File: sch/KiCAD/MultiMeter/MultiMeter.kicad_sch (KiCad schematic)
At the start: 27 parts, among them J1 Conn_01x02_Male, J2 Conn_01x02_Male, J3 Conn_01x03_Male, J4 Conn_01x03_Male, J5 Conn_01x02_Female, J6 Conn_01x15, J7 Conn_01x15, J8 Conn_01x08_Female, Q1 2SC1815, Q2 2SC1815

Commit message: 回路図修正
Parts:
- added J9: (no value), symbol Connector:Conn_01x02_Male
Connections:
- net GNDPWR: now also J9.2 (Pin_2)
- net +12V: now reaches A1.30 (VIN), J7.15 (Pin_15)
- net +12V: now also J9.1 (Pin_1)
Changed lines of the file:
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@@
   (junction (at 83.82 52.07) (diameter 0) (color 0 0 0 0)
   )
+  (junction (at 111.76 26.67) (diameter 0) (color 0 0 0 0)
+  )
   (junction (at 133.35 72.39) (diameter 0) (color 0 0 0 0)
   )
@@
     (stroke (width 0) (type default) (color 0 0 0 0))
   )
+  (wire (pts (xy 110.49 176.53) (xy 110.49 167.64))
+    (stroke (width 0) (type default) (color 0 0 0 0))
+  )
   (wire (pts (xy 116.84 25.4) (xy 139.7 25.4))
     (stroke (width 0) (type default) (color 0 0 0 0))
@@
     (stroke (width 0) (type default) (color 0 0 0 0))
   )
+  (wire (pts (xy 110.49 167.64) (xy 121.92 167.64))
+    (stroke (width 0) (type default) (color 0 0 0 0))
+  )
   (wire (pts (xy 50.8 34.29) (xy 50.8 45.72))
     (stroke (width 0) (type default) (color 0 0 0 0))
@@
     (stroke (width 0) (type default) (color 0 0 0 0))
   )
+  (wire (pts (xy 85.09 20.32) (xy 85.09 22.86))
+    (stroke (width 0) (type default) (color 0 0 0 0))
+  )
   (wire (pts (xy 133.35 72.39) (xy 149.86 72.39))
     (stroke (width 0) (type default) (color 0 0 0 0))
@@
     (stroke (width 0) (type default) (color 0 0 0 0))
   )
+  (wire (pts (xy 111.76 20.32) (xy 85.09 20.32))
+    (stroke (width 0) (type default) (color 0 0 0 0))
+  )
   (wire (pts (xy 173.99 67.31) (xy 173.99 78.74))
     (stroke (width 0) (type default) (color 0 0 0 0))
@@
     (stroke (width 0) (type default) (color 0 0 0 0))
   )
+  (wire (pts (xy 97.79 176.53) (xy 97.79 165.1))
+    (stroke (width 0) (type default) (color 0 0 0 0))
+  )
   (wire (pts (xy 97.79 80.01) (xy 97.79 106.68))
     (stroke (width 0) (type default) (color 0 0 0 0))
@@
     (stroke (width 0) (type default) (color 0 0 0 0))
   )
+  (wire (pts (xy 111.76 26.67) (xy 111.76 20.32))
+    (stroke (width 0) (type default) (color 0 0 0 0))
+  )
   (wire (pts (xy 44.45 62.23) (xy 44.45 60.96))
+    (stroke (width 0) (type default) (color 0 0 0 0))
+  )
+  (wire (pts (xy 97.79 165.1) (xy 121.92 165.1))
     (stroke (width 0) (type default) (color 0 0 0 0))
   )
@@
     (pin "2")
   )
+  (symbol (lib_id "power:+12V") (at 97.79 176.53 0) (mirror x) (unit 1)
+    (in_bom yes) (on_board yes) (fields_autoplaced)
+    (property "Reference" "#PWR0117" (id 0) (at 97.79 172.72 0)
+      (effects (font (size 1.27 1.27)) hide)
+    )
+    (property "Value" "+12V" (id 1) (at 97.79 181.61 0))
+    (property "Footprint" "" (id 2) (at 97.79 176.53 0)
+      (effects (font (size 1.27 1.27)) hide)
+    )
+    (property "Datasheet" "" (id 3) (at 97.79 176.53 0)
+      (effects (font (size 1.27 1.27)) hide)
+    )
+    (pin "1")
+  )
   (symbol (lib_id "power:GNDPWR") (at 58.42 77.47 0) (unit 1)
     (in_bom yes) (on_board yes) (fields_autoplaced)
@@
     )
     (property "Datasheet" "" (id 3) (at 173.99 88.9 0)
+      (effects (font (size 1.27 1.27)) hide)
+    )
+    (pin "1")
+  )
+  (symbol (lib_id "power:+12V") (at 85.09 22.86 0) (mirror x) (unit 1)
+    (in_bom yes) (on_board yes) (fields_autoplaced)
+    (property "Reference" "#PWR0116" (id 0) (at 85.09 19.05 0)
+      (effects (font (size 1.27 1.27)) hide)
+    )
+    (property "Value" "+12V" (id 1) (at 85.09 27.94 0))
+    (property "Footprint" "" (id 2) (at 85.09 22.86 0)
+      (effects (font (size 1.27 1.27)) hide)
+    )
+    (property "Datasheet" "" (id 3) (at 85.09 22.86 0)
       (effects (font (size 1.27 1.27)) hide)
     )
@@
     (pin "1")
   )
+  (symbol (lib_id "power:GNDPWR") (at 110.49 176.53 0) (unit 1)
+    (in_bom yes) (on_board yes) (fields_autoplaced)
+    (property "Reference" "#PWR0118" (id 0) (at 110.49 181.61 0)
+      (effects (font (size 1.27 1.27)) hide)
+    )
+    (property "Value" "GNDPWR" (id 1) (at 110.363 181.61 0))
+    (property "Footprint" "" (id 2) (at 110.49 177.8 0)
+      (effects (font (size 1.27 1.27)) hide)
+    )
+    (property "Datasheet" "" (id 3) (at 110.49 177.8 0)
+      (effects (font (size 1.27 1.27)) hide)
+    )
+    (pin "1")
+  )
   (symbol (lib_id "power:+5V") (at 154.94 90.17 180) (unit 1)
     (in_bom yes) (on_board yes) (fields_autoplaced)
@@
     (pin "2")
   )
+  (symbol (lib_id "Connector:Conn_01x02_Male") (at 127 165.1 0) (mirror y) (unit 1)
+    (in_bom yes) (on_board yes) (fields_autoplaced)
+    (property "Reference" "J9" (id 0) (at 128.27 165.0999 0)
+      (effects (font (size 1.27 1.27)) (justify right))
+    )
+    (property "Value" "" (id 1) (at 128.27 167.6399 0)
+      (effects (font (size 1.27 1.27)) (justify right))
+    )
+    (property "Footprint" "" (id 2) (at 127 165.1 0)
+      (effects (font (size 1.27 1.27)) hide)
+    )
+    (property "Datasheet" "~" (id 3) (at 127 165.1 0)
+      (effects (font (size 1.27 1.27)) hide)
+    )
+    (pin "1")
+    (pin "2")
+  )
   (symbol (lib_id "power:+5V") (at 171.45 137.16 180) (unit 1)
     (in_bom yes) (on_board yes) (fields_autoplaced)
@@
       (reference "#PWR0115") (unit 1) (value "GNDPWR") (footprint "")
     )
+    (path "/572bf966-40b4-4074-84f8-0470619143e0"
+      (reference "#PWR0116") (unit 1) (value "+12V") (footprint "")
+    )
+    (path "/2764df4e-6524-4e92-b3c2-377361d2725a"
+      (reference "#PWR0117") (unit 1) (value "+12V") (footprint "")
+    )
+    (path "/bcc17d3a-2a6b-4226-83a3-ee2299dfa9ff"
+      (reference "#PWR0118") (unit 1) (value "GNDPWR") (footprint "")
+    )
     (path "/b8413942-d6c5-419c-abde-ad0808ce4040"
       (reference "A1") (unit 1) (value "Arduino_Nano_v3.x") (footprint "Module:Arduino_Nano")
@@
       (reference "J8") (unit 1) (value "Conn_01x08_Female") (footprint "Connector_JST:JST_XH_B8B-XH-A_1x08_P2.50mm_Vertical")
     )
+    (path "/cd4406c8-1d31-4759-9e62-d689d76eb5ee"
+      (reference "J9") (unit 1) (value "Conn_01x02_Female") (footprint "Connector_Molex:Molex_KK-254_AE-6410-02A_1x02_P2.54mm_Vertical")
+    )
     (path "/6516d9f9-5a5c-40a3-bbc8-e5224e1e784c"

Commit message: 回路図修正
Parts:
- removed R10: 7K ohm, Resistor_THT:R_Axial_DIN0204_L3.6mm_D1.6mm_P7.62mm_Horizontal, symbol Device:R
- removed R11: 5K ohm, Resistor_THT:R_Axial_DIN0204_L3.6mm_D1.6mm_P7.62mm_Horizontal, symbol Device:R
- removed TP1, TP2: TestPoint, MountingHole:MountingHole_2.2mm_M2_DIN965_Pad, symbol Connector:TestPoint
- J5: value Conn_01x02_Female -> (none); footprint Connector_Molex:Molex_KK-254_AE-6410-02A_1x02_P2.54mm_Vertical -> (none); symbol Connector:Conn_01x02_Female -> Connector:Conn_01x03_Female
- J9: value (none) -> Conn_01x02_Female; footprint (none) -> Connector_Molex:Molex_KK-254_AE-6410-02A_1x02_P2.54mm_Vertical; symbol Connector:Conn_01x02_Male -> Connector:Conn_01x03_Female
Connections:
- net +12V: now also J9.2 (Pin_2), RV1.1; no longer J9.1 (Pin_1)
- net +5V: no longer RV1.1
- net GNDPWR: now also J9.3 (Pin_3), Q2.3 (B), R9.2; no longer J9.2 (Pin_2)
- net at A1.23 (A4), J7.8 (Pin_8), J8.4 (Pin_4): no longer J4.2 (Pin_2)
- net at A1.25 (A6), J7.10 (Pin_10): now also J4.2 (Pin_2)
- net at A1.26 (A7), J7.11 (Pin_11): now also J5.3 (Pin_3)
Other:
- moved on the sheet: A1, D5, J1, J2, J3, J4, J6, J7, J8, JP1, Q1, Q2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

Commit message: 回路図修正
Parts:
- J5: value (none) -> Conn_01x03_Female; footprint (none) -> Connector_Molex:Molex_KK-254_AE-6410-03A_1x03_P2.54mm_Vertical
- J9: value Conn_01x02_Female -> (none); footprint Connector_Molex:Molex_KK-254_AE-6410-02A_1x02_P2.54mm_Vertical -> (none); symbol Connector:Conn_01x03_Female -> Connector:Conn_01x02_Female
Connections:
- net +12V: now also J9.1 (Pin_1); no longer J9.2 (Pin_2)
- net GNDPWR: now also J9.2 (Pin_2); no longer J9.3 (Pin_3)
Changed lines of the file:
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@@
     (in_bom yes) (on_board yes)
     (property "Reference" "J5" (id 0) (at 33.655 59.69 0))
-    (property "Value" "" (id 1) (at 33.02 55.88 0))
-    (property "Footprint" "" (id 2) (at 33.02 64.77 0)
+    (property "Value" "Conn_01x03_Female" (id 1) (at 33.02 55.88 0))
+    (property "Footprint" "Connector_Molex:Molex_KK-254_AE-6410-03A_1x03_P2.54mm_Vertical" (id 2) (at 33.02 64.77 0)
       (effects (font (size 1.27 1.27)) hide)
     )
@@
     (pin "2")
   )
-  (symbol (lib_id "Connector:Conn_01x03_Female") (at 127 165.1 0) (unit 1)
+  (symbol (lib_id "Connector:Conn_01x02_Female") (at 127 165.1 0) (unit 1)
     (in_bom yes) (on_board yes)
     (property "Reference" "J9" (id 0) (at 128.27 158.75 0)
       (effects (font (size 1.27 1.27)) (justify right))
     )
-    (property "Value" "Conn_01x02_Female" (id 1) (at 137.16 172.72 0)
+    (property "Value" "" (id 1) (at 137.16 172.72 0)
       (effects (font (size 1.27 1.27)) (justify right))
     )
-    (property "Footprint" "Connector_Molex:Molex_KK-254_AE-6410-02A_1x02_P2.54mm_Vertical" (id 2) (at 127 165.1 0)
+    (property "Footprint" "" (id 2) (at 127 165.1 0)
       (effects (font (size 1.27 1.27)) hide)
     )
@@
     (pin "1")
     (pin "2")
-    (pin "3")
   )
   (symbol (lib_id "power:+5V") (at 187.96 142.24 180) (unit 1)

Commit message: 回路図更新
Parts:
- added J10: (no value), symbol Connector:Conn_01x04_Female
- J8: value Conn_01x08_Female -> (none); footprint Connector_JST:JST_XH_B8B-XH-A_1x08_P2.50mm_Vertical -> (none)
- J9: value (none) -> Conn_01x02_Female; footprint (none) -> Connector_Molex:Molex_KK-254_AE-6410-02A_1x02_P2.54mm_Vertical
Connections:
- net +5V: now also J10.1 (Pin_1)
- net GNDPWR: now also J10.4 (Pin_4)
- net at A1.1 (D1/TX), J6.1 (Pin_1): now also J10.3 (Pin_3)
- net at A1.2 (D0/RX), J6.2 (Pin_2): now also J10.2 (Pin_2)
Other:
- moved on the sheet: D5, R5

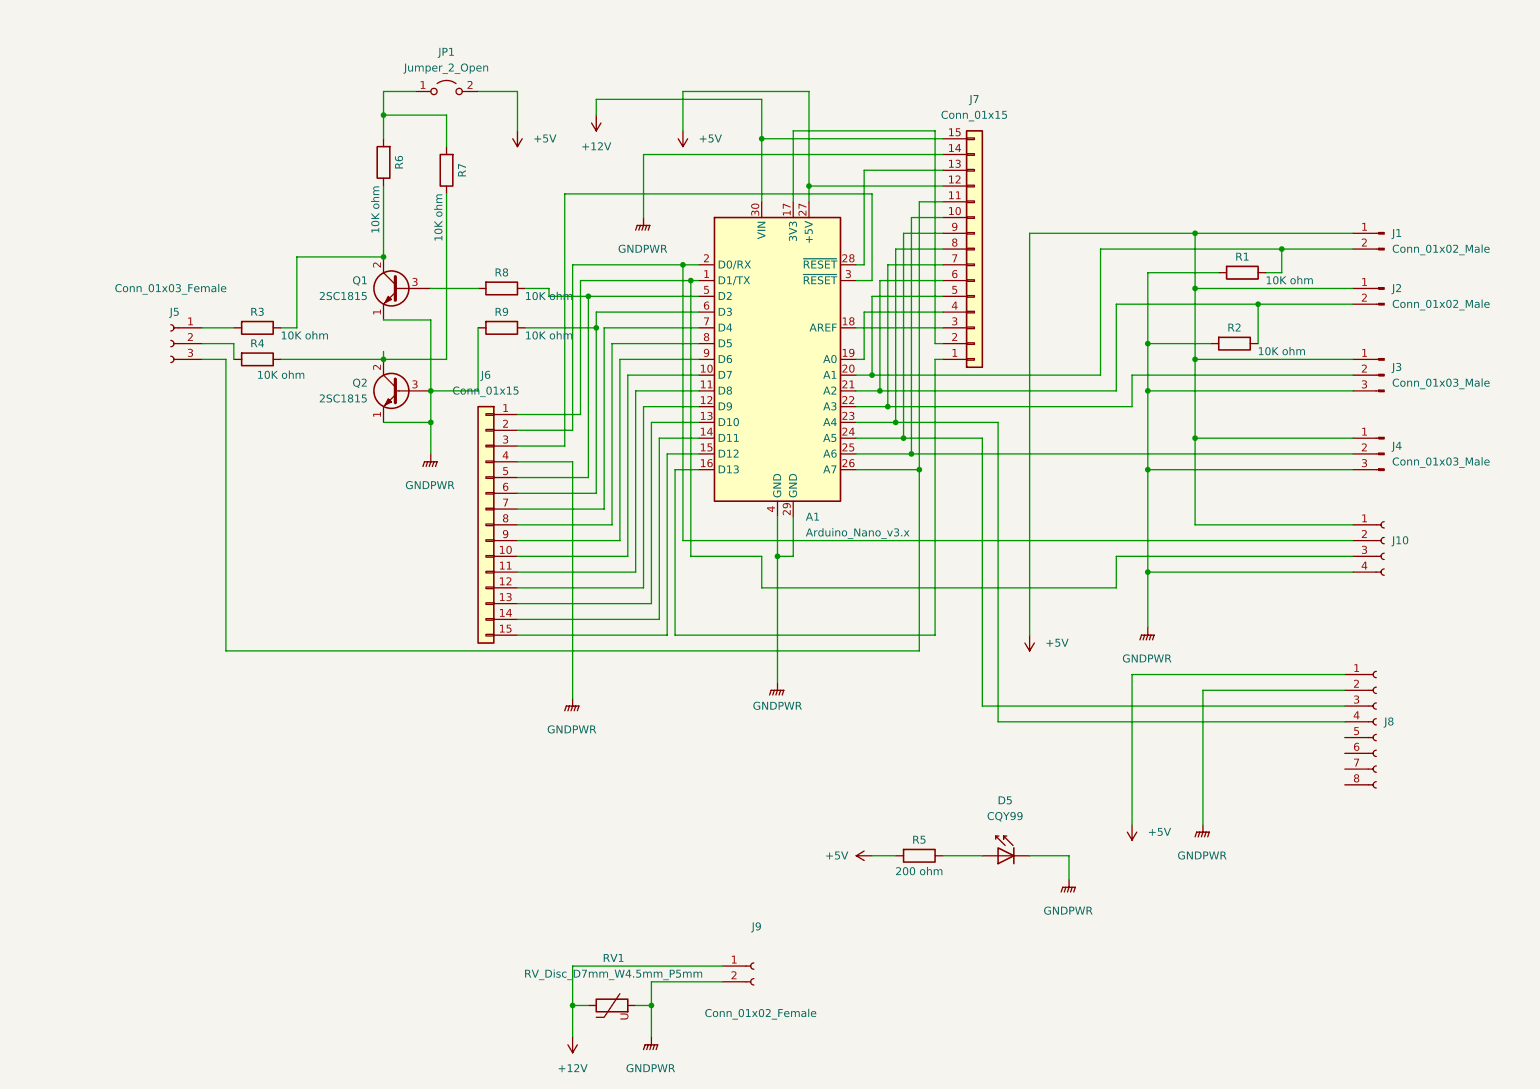
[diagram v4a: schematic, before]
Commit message: 回路図、パターンを修正
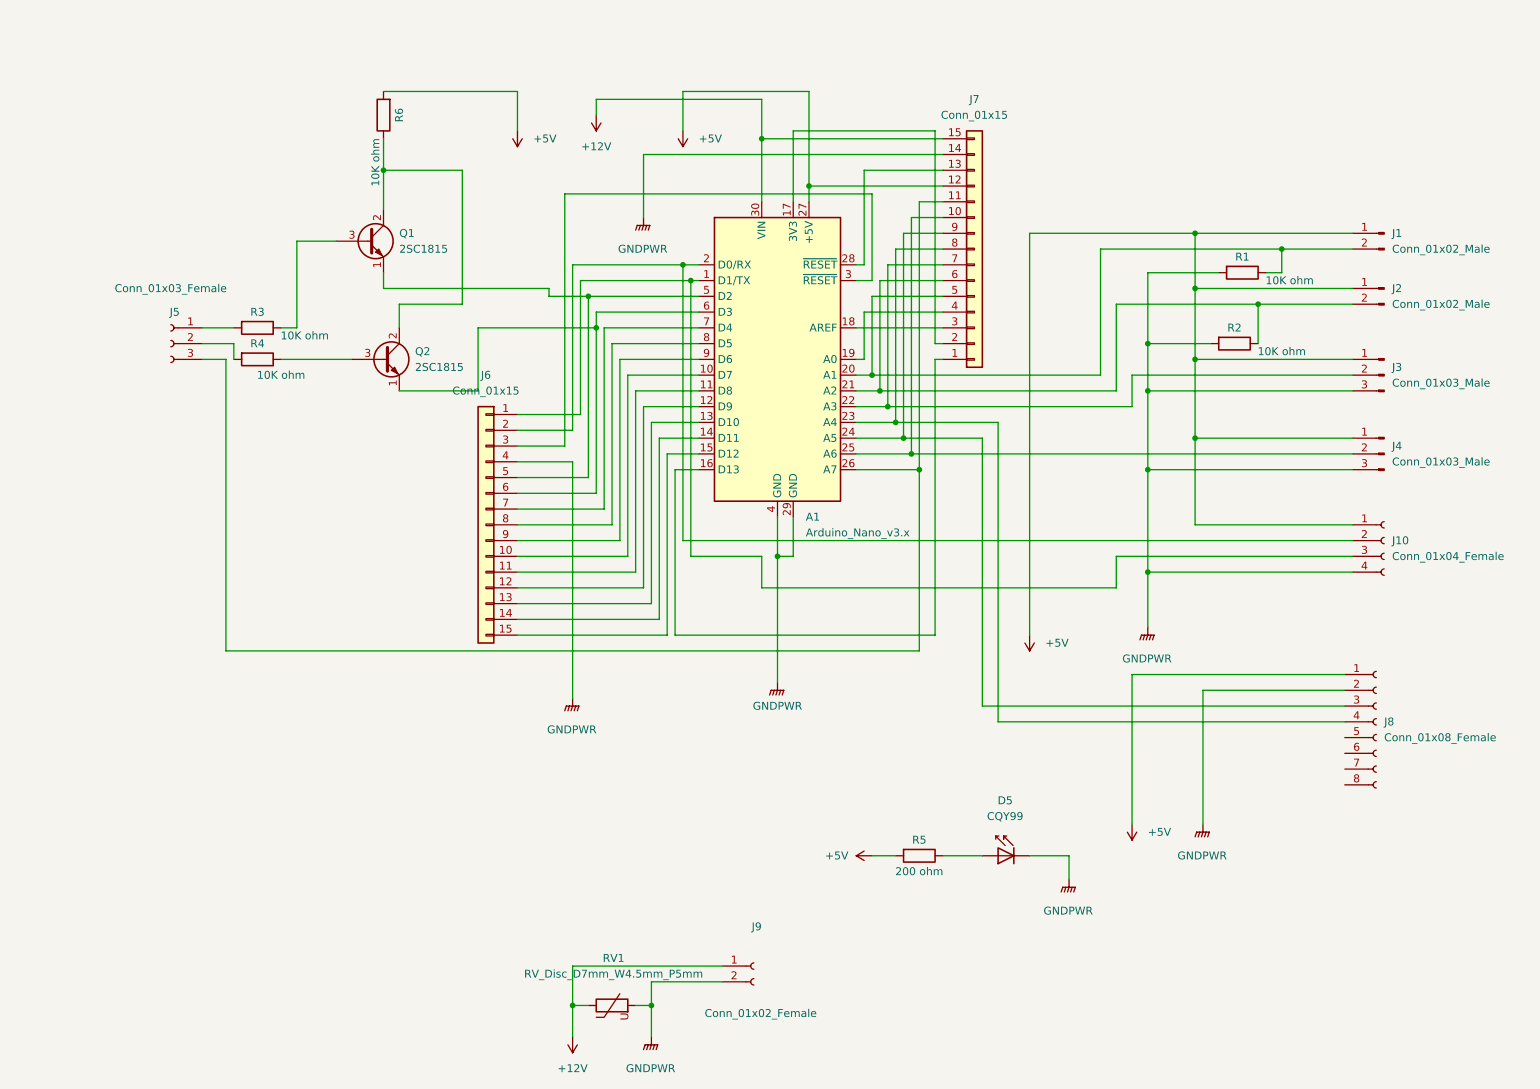
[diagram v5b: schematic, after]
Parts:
- removed JP1: Jumper_2_Open, Connector_PinHeader_2.54mm:PinHeader_1x02_P2.54mm_Vertical, symbol Jumper:Jumper_2_Open
- removed R7, R8, R9: 10K ohm, Resistor_THT:R_Axial_DIN0204_L3.6mm_D1.6mm_P7.62mm_Horizontal, symbol Device:R
- J10: value (none) -> Conn_01x04_Female; footprint (none) -> Connector_Molex:Molex_SPOX_5268-04A_1x04_P2.50mm_Horizontal
- J8: value (none) -> Conn_01x08_Female; footprint (none) -> Connector_JST:JST_XH_S8B-XH-A-1_1x08_P2.50mm_Horizontal
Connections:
- net +5V: now also R6.2
- net GNDPWR: no longer Q1.1 (E), Q2.1 (E), Q2.3 (B)
- net at R4.1: now also Q2.3 (B); no longer Q2.2 (C)
- net at Q1.2 (C), R6.1: now also Q2.2 (C); no longer R3.1
- net at A1.5 (D2), J6.5 (Pin_5): now also Q1.1 (E)
- net at A1.6 (D3), J6.6 (Pin_6): now also Q2.1 (E)
- net at Q1.3 (B): now also R3.1
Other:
- moved on the sheet: Q1, Q2, R6
